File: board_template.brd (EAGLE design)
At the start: 51.6 x 108 mm, 1 part

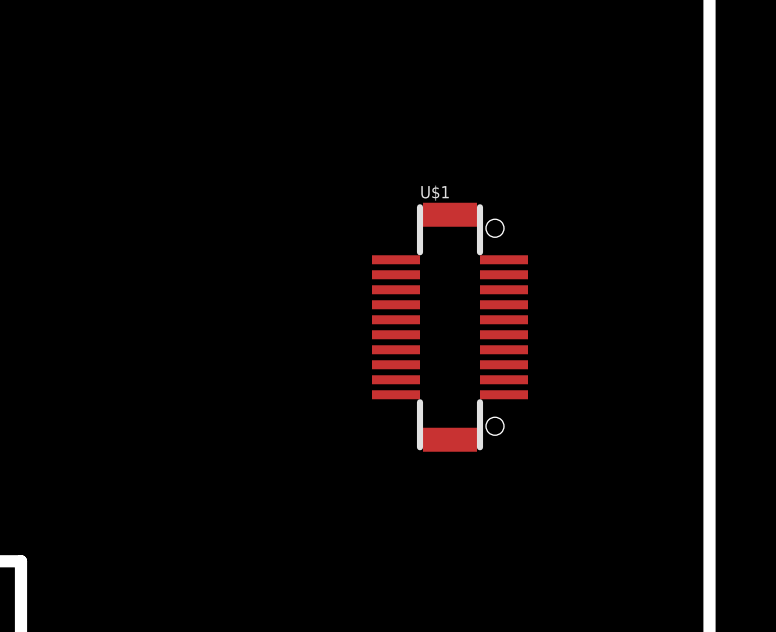
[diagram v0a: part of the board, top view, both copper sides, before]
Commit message: moved df12-ds20 connectro to bottom layer
I revied the desgnes and relised that the connector should go on the bottom with
a keep out zone on the top layer above it. I have updated the template to reflect
this
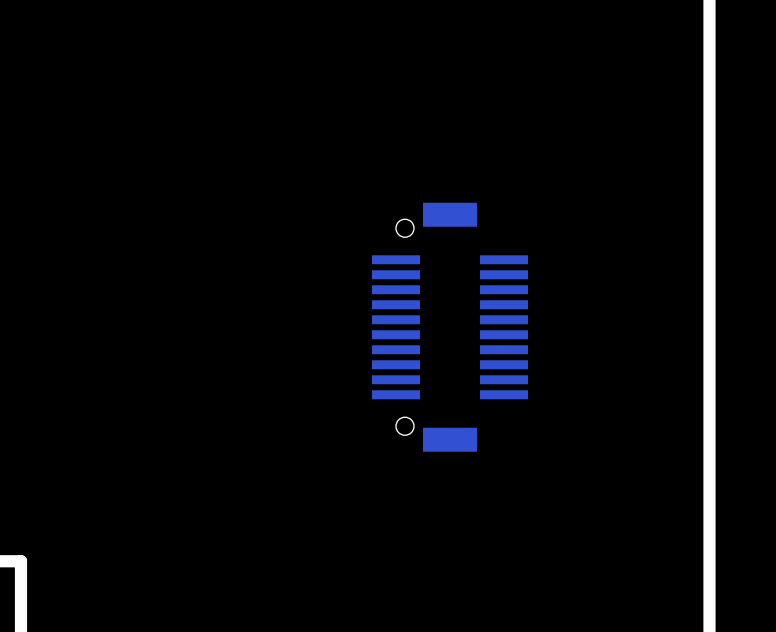
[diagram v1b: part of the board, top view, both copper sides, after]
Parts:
- flipped U$1 to the bottom
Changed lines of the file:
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@@
 <vertex x="10.8" y="31.56"/>
+</polygon>
+<polygon width="0.4064" layer="39">
+<vertex x="40" y="21"/>
+<vertex x="46" y="21"/>
+<vertex x="46" y="11.5"/>
+<vertex x="40" y="11.5"/>
 </polygon>
 </plain>
@@
 </autorouter>
 <elements>
-<element name="U$1" library="tribesat" package="DF12(3.0)-20DS-0.5V(86)" value="DF12-20DS" x="42.93" y="16.3"/>
+<element name="U$1" library="tribesat" package="DF12(3.0)-20DS-0.5V(86)" value="DF12-20DS" x="42.93" y="16.3" rot="MR0"/>
 </elements>
 <signals>
